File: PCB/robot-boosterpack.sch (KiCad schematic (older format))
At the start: 12 parts

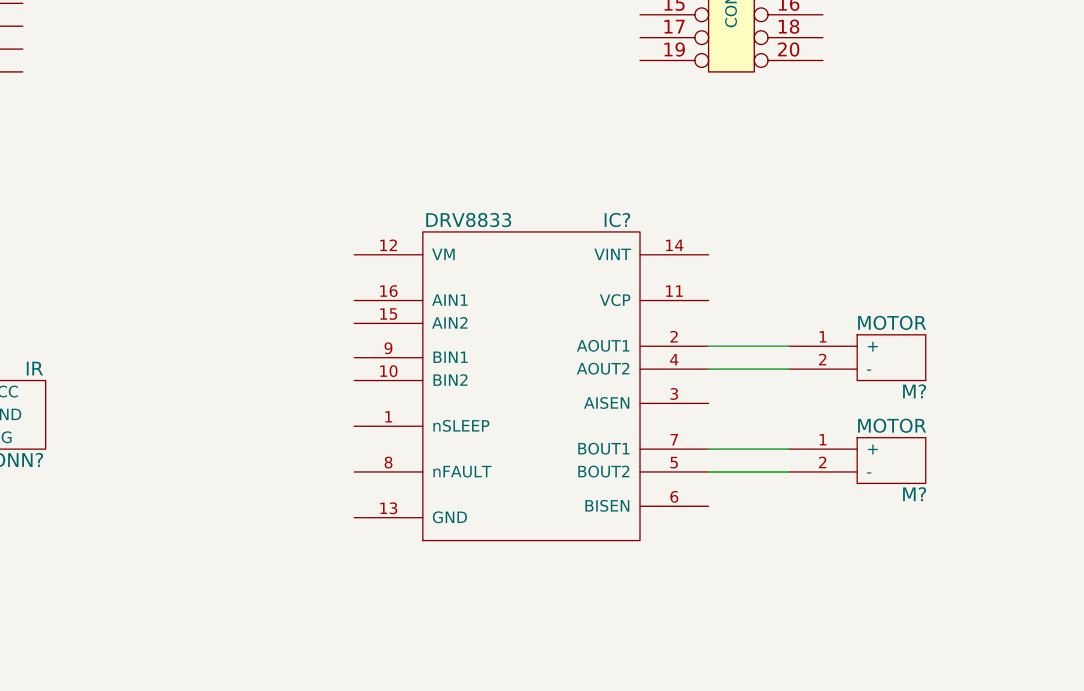
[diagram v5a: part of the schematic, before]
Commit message: created motor controller circuit
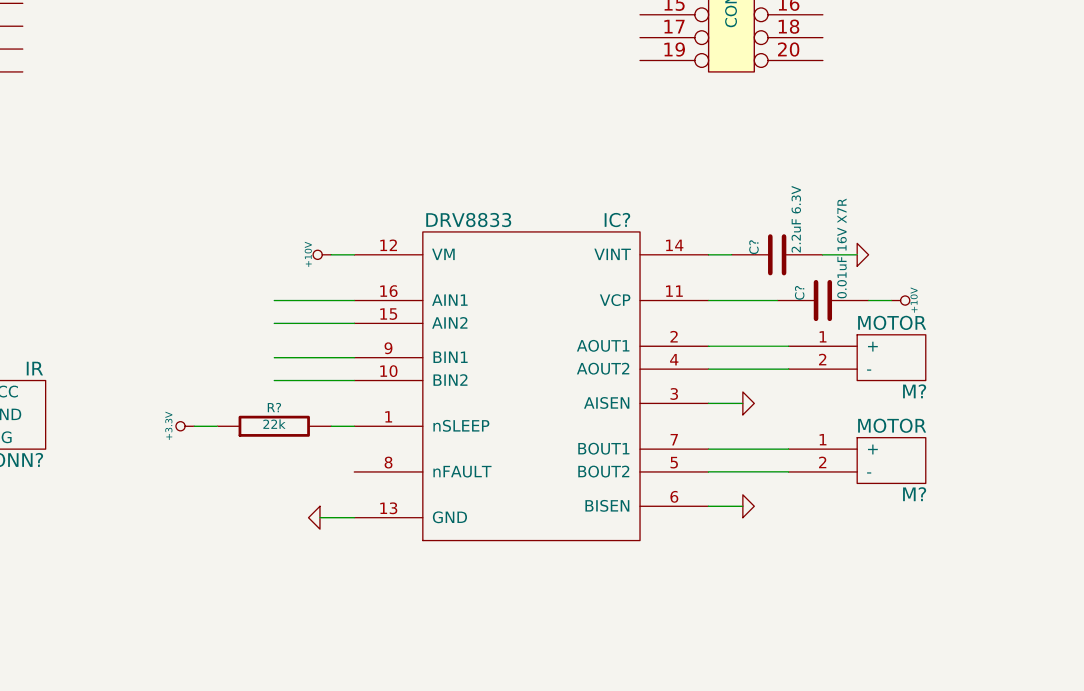
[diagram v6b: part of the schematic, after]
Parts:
- added C?: 0.01uF 16V X7R, ~, symbol C
- added C?: 2.2uF 6.3V, ~, symbol C
- added R?: 22k, ~, symbol R
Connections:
- net labels added: +10V
- wire segments 26 -> 40
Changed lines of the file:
@@
 	7150 1700 7150 1600
 Connection ~ 7150 1600
+$Comp
+L GND #PWR?
+U 1 1 53A79425
+P 5700 6000
+F 0 "#PWR?" H 5700 6000 30  0001 C CNN
+F 1 "GND" H 5700 5930 30  0001 C CNN
+F 2 "" H 5700 6000 60  0000 C CNN
+F 3 "" H 5700 6000 60  0000 C CNN
+	1    5700 6000
+	0    1    1    0
+$EndComp
+Wire Wire Line
+	5850 6000 5700 6000
+$Comp
+L GND #PWR?
+U 1 1 53A79483
+P 7550 5950
+F 0 "#PWR?" H 7550 5950 30  0001 C CNN
+F 1 "GND" H 7550 5880 30  0001 C CNN
+F 2 "" H 7550 5950 60  0000 C CNN
+F 3 "" H 7550 5950 60  0000 C CNN
+	1    7550 5950
+	0    -1   -1   0
+$EndComp
+$Comp
+L GND #PWR?
+U 1 1 53A79489
+P 7550 5500
+F 0 "#PWR?" H 7550 5500 30  0001 C CNN
+F 1 "GND" H 7550 5430 30  0001 C CNN
+F 2 "" H 7550 5500 60  0000 C CNN
+F 3 "" H 7550 5500 60  0000 C CNN
+	1    7550 5500
+	0    -1   -1   0
+$EndComp
+Wire Wire Line
+	7400 5500 7550 5500
+Wire Wire Line
+	7400 5950 7550 5950
+$Comp
+L C C?
+U 1 1 53A7958C
+P 7900 5050
+F 0 "C?" H 7900 5150 40  0000 L CNN
+F 1 "0.01uF 16V X7R" H 7906 4965 40  0000 L CNN
+F 2 "~" H 7938 4900 30  0000 C CNN
+F 3 "~" H 7900 5050 60  0000 C CNN
+	1    7900 5050
+	0    -1   -1   0
+$EndComp
+Wire Wire Line
+	7400 5050 7700 5050
+$Comp
+L C C?
+U 1 1 53A795DA
+P 7700 4850
+F 0 "C?" H 7700 4950 40  0000 L CNN
+F 1 "2.2uF 6.3V" H 7706 4765 40  0000 L CNN
+F 2 "~" H 7738 4700 30  0000 C CNN
+F 3 "~" H 7700 4850 60  0000 C CNN
+	1    7700 4850
+	0    -1   -1   0
+$EndComp
+Wire Wire Line
+	7400 4850 7500 4850
+$Comp
+L GND #PWR?
+U 1 1 53A7963B
+P 8050 4850
+F 0 "#PWR?" H 8050 4850 30  0001 C CNN
+F 1 "GND" H 8050 4780 30  0001 C CNN
+F 2 "" H 8050 4850 60  0000 C CNN
+F 3 "" H 8050 4850 60  0000 C CNN
+	1    8050 4850
+	0    -1   -1   0
+$EndComp
+Wire Wire Line
+	8050 4850 7900 4850
+$Comp
+L +10V #PWR?
+U 1 1 53A798E9
+P 5750 4850
+F 0 "#PWR?" H 5750 4800 20  0001 C CNN
+F 1 "+10V" H 5750 4950 30  0000 C CNN
+F 2 "" H 5750 4850 60  0000 C CNN
+F 3 "" H 5750 4850 60  0000 C CNN
+	1    5750 4850
+	0    -1   -1   0
+$EndComp
+Wire Wire Line
+	5850 4850 5750 4850
+$Comp
+L +10V #PWR?
+U 1 1 53A7993E
+P 8200 5050
+F 0 "#PWR?" H 8200 5000 20  0001 C CNN
+F 1 "+10V" H 8200 5150 30  0000 C CNN
+F 2 "" H 8200 5050 60  0000 C CNN
+F 3 "" H 8200 5050 60  0000 C CNN
+	1    8200 5050
+	0    1    1    0
+$EndComp
+Wire Wire Line
+	8200 5050 8100 5050
+Wire Wire Line
+	5850 5050 5500 5050
+Wire Wire Line
+	5850 5150 5500 5150
+Wire Wire Line
+	5850 5300 5500 5300
+Wire Wire Line
+	5850 5400 5500 5400
+$Comp
+L R R?
+U 1 1 53A79B05
+P 5500 5600
+F 0 "R?" V 5580 5600 40  0000 C CNN
+F 1 "22k" V 5507 5601 40  0000 C CNN
+F 2 "~" V 5430 5600 30  0000 C CNN
+F 3 "~" H 5500 5600 30  0000 C CNN
+	1    5500 5600
+	0    -1   -1   0
+$EndComp
+Wire Wire Line
+	5750 5600 5850 5600
+$Comp
+L +3.3V #PWR?
+U 1 1 53A79B60
+P 5150 5600
+F 0 "#PWR?" H 5150 5560 30  0001 C CNN
+F 1 "+3.3V" H 5150 5710 30  0000 C CNN
+F 2 "" H 5150 5600 60  0000 C CNN
+F 3 "" H 5150 5600 60  0000 C CNN
+	1    5150 5600
+	0    -1   -1   0
+$EndComp
+Wire Wire Line
+	5150 5600 5250 5600
 $EndSCHEMATC

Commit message: Misc changes
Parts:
- added C?: 10uF, ~, symbol C
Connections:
- wire segments 40 -> 43
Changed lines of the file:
@@
 L +10V #PWR?
 U 1 1 53A798E9
-P 5750 4850
-F 0 "#PWR?" H 5750 4800 20  0001 C CNN
-F 1 "+10V" H 5750 4950 30  0000 C CNN
-F 2 "" H 5750 4850 60  0000 C CNN
-F 3 "" H 5750 4850 60  0000 C CNN
-	1    5750 4850
+P 5400 4850
+F 0 "#PWR?" H 5400 4800 20  0001 C CNN
+F 1 "+10V" H 5400 4950 30  0000 C CNN
+F 2 "" H 5400 4850 60  0000 C CNN
+F 3 "" H 5400 4850 60  0000 C CNN
+	1    5400 4850
 	0    -1   -1   0
 $EndComp
 Wire Wire Line
-	5850 4850 5750 4850
+	5400 4850 5850 4850
 $Comp
 L +10V #PWR?
@@
 Wire Wire Line
 	5150 5600 5250 5600
+$Comp
+L C C?
+U 1 1 53A79C6C
+P 5600 4650
+F 0 "C?" H 5600 4750 40  0000 L CNN
+F 1 "10uF" H 5606 4565 40  0000 L CNN
+F 2 "~" H 5638 4500 30  0000 C CNN
+F 3 "~" H 5600 4650 60  0000 C CNN
+	1    5600 4650
+	1    0    0    -1
+$EndComp
+Connection ~ 5600 4850
+$Comp
+L GND #PWR?
+U 1 1 53A79CCB
+P 5800 4500
+F 0 "#PWR?" H 5800 4500 30  0001 C CNN
+F 1 "GND" H 5800 4430 30  0001 C CNN
+F 2 "" H 5800 4500 60  0000 C CNN
+F 3 "" H 5800 4500 60  0000 C CNN
+	1    5800 4500
+	1    0    0    -1
+$EndComp
+Wire Wire Line
+	5800 4500 5800 4350
+Wire Wire Line
+	5800 4350 5600 4350
+Wire Wire Line
+	5600 4350 5600 4450
 $EndSCHEMATC

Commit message: added 3.3V regulator part
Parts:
- added IC?: TPS77033, symbol TPS77033
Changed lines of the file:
@@
 LIBS:robot-boosterpack
 LIBS:robot-boosterpack-cache
-EELAYER 27 0
+EELAYER 24 0
 EELAYER END
 $Descr A4 11693 8268
@@
 Wire Wire Line
 	5600 4350 5600 4450
+$Comp
+L TPS77033 IC?
+U 1 1 53A8A5F0
+P 4700 1800
+F 0 "IC?" H 4950 2100 60  0000 C CNN
+F 1 "TPS77033" H 4550 2100 60  0000 C CNN
+F 2 "" H 4550 2100 60  0000 C CNN
+F 3 "" H 4550 2100 60  0000 C CNN
+	1    4700 1800
+	1    0    0    -1
+$EndComp
 $EndSCHEMATC
